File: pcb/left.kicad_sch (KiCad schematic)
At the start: 53 parts, among them J101 B12B-PHDSS, SW10 SW_Push, SW11 SW_Push, SW12 SW_Push, SW13 SW_Push, SW15 SW_Push, SW16 SW_Push, SW17 SW_Push, SW18 SW_Push, SW19 SW_Push, SW20 SW_Push, SW22 SW_Push, SW23 SW_Push, SW24 SW_Push, SW25 SW_Push, SW26 SW_Push, SW27 SW_Push, SW28 SW_Push, SW29 SW_Push, SW30 SW_Push, SW31 SW_Push, SW32 SW_Push, SW33 SW_Push, SW34 SW_Push, SW35 SW_Push, SW8 SW_Push, SW9 SW_Push

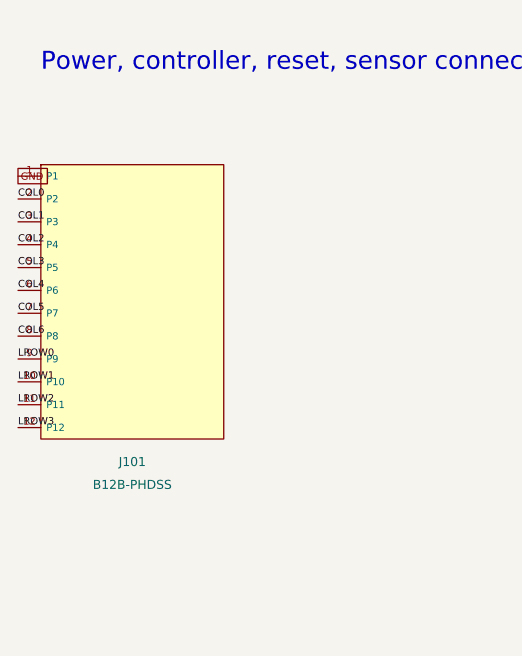
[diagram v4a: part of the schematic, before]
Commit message: Replace split connectors with Samtec FFSD-compatible headers
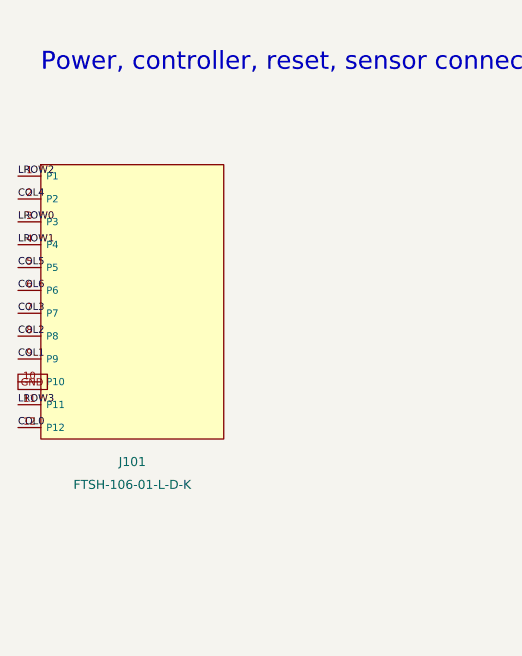
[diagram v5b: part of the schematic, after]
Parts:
- J101: value B12B-PHDSS -> FTSH-106-01-L-D-K; footprint Connector_JST:JST_PHD_B12B-PHDSS_2x06_P2.00mm_Vertical -> Library:Samtec_FTSH-106-01-L-D-K
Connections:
- net COL0: now also J101.12 (P12); no longer J101.2 (P2)
- net COL1: now also J101.9 (P9); no longer J101.3 (P3)
- net COL2: now also J101.8 (P8); no longer J101.4 (P4)
- net COL3: now also J101.7 (P7); no longer J101.5 (P5)
- net COL4: now also J101.2 (P2); no longer J101.6 (P6)
- net COL5: now also J101.5 (P5); no longer J101.7 (P7)
- net COL6: now also J101.6 (P6); no longer J101.8 (P8)
- net GND: now also J101.10 (P10); no longer J101.1 (P1)
- net LROW0: now also J101.3 (P3); no longer J101.9 (P9)
- net LROW1: now also J101.4 (P4); no longer J101.10 (P10)
- net LROW2: now also J101.1 (P1); no longer J101.11 (P11)
- net LROW3: now also J101.11 (P11); no longer J101.12 (P12)
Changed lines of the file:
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@@
 			(effects (font (size 1.0 1.0)))
 		)
-		(property "Value" "B12B-PHDSS"
+		(property "Value" "FTSH-106-01-L-D-K"
 			(at 22.860 205.740 0)
 			(effects (font (size 1.0 1.0)))
 		)
-		(property "Footprint" "Connector_JST:JST_PHD_B12B-PHDSS_2x06_P2.00mm_Vertical"
+		(property "Footprint" "Library:Samtec_FTSH-106-01-L-D-K"
 			(at 22.860 185.420 0)
 			(effects (font (size 1.0 1.0)) (hide yes))
@@
 		)
 	)
+	(label "LROW2"
+		(at 10.160 171.450 0)
+		(effects (font (size 0.8 0.8)) (justify left bottom))
+	)
+	(label "COL4"
+		(at 10.160 173.990 0)
+		(effects (font (size 0.8 0.8)) (justify left bottom))
+	)
+	(label "LROW0"
+		(at 10.160 176.530 0)
+		(effects (font (size 0.8 0.8)) (justify left bottom))
+	)
+	(label "LROW1"
+		(at 10.160 179.070 0)
+		(effects (font (size 0.8 0.8)) (justify left bottom))
+	)
+	(label "COL5"
+		(at 10.160 181.610 0)
+		(effects (font (size 0.8 0.8)) (justify left bottom))
+	)
+	(label "COL6"
+		(at 10.160 184.150 0)
+		(effects (font (size 0.8 0.8)) (justify left bottom))
+	)
+	(label "COL3"
+		(at 10.160 186.690 0)
+		(effects (font (size 0.8 0.8)) (justify left bottom))
+	)
+	(label "COL2"
+		(at 10.160 189.230 0)
+		(effects (font (size 0.8 0.8)) (justify left bottom))
+	)
+	(label "COL1"
+		(at 10.160 191.770 0)
+		(effects (font (size 0.8 0.8)) (justify left bottom))
+	)
 	(global_label "GND"
 		(shape passive)
-		(at 10.160 171.450 0)
+		(at 10.160 194.310 0)
 		(fields_autoplaced yes)
 		(effects (font (size 0.8 0.8)) (justify left bottom))
 	)
-	(label "COL0"
-		(at 10.160 173.990 0)
-		(effects (font (size 0.8 0.8)) (justify left bottom))
-	)
-	(label "COL1"
-		(at 10.160 176.530 0)
-		(effects (font (size 0.8 0.8)) (justify left bottom))
-	)
-	(label "COL2"
-		(at 10.160 179.070 0)
-		(effects (font (size 0.8 0.8)) (justify left bottom))
-	)
-	(label "COL3"
-		(at 10.160 181.610 0)
-		(effects (font (size 0.8 0.8)) (justify left bottom))
-	)
-	(label "COL4"
-		(at 10.160 184.150 0)
-		(effects (font (size 0.8 0.8)) (justify left bottom))
-	)
-	(label "COL5"
-		(at 10.160 186.690 0)
-		(effects (font (size 0.8 0.8)) (justify left bottom))
-	)
-	(label "COL6"
-		(at 10.160 189.230 0)
-		(effects (font (size 0.8 0.8)) (justify left bottom))
-	)
-	(label "LROW0"
-		(at 10.160 191.770 0)
-		(effects (font (size 0.8 0.8)) (justify left bottom))
-	)
-	(label "LROW1"
-		(at 10.160 194.310 0)
-		(effects (font (size 0.8 0.8)) (justify left bottom))
-	)
-	(label "LROW2"
+	(label "LROW3"
 		(at 10.160 196.850 0)
 		(effects (font (size 0.8 0.8)) (justify left bottom))
 	)
-	(label "LROW3"
+	(label "COL0"
 		(at 10.160 199.390 0)
 		(effects (font (size 0.8 0.8)) (justify left bottom))
